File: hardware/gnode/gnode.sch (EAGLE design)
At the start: 20 parts, among them IC1 HTU21D, U1 ATMEGA328P_TQFP

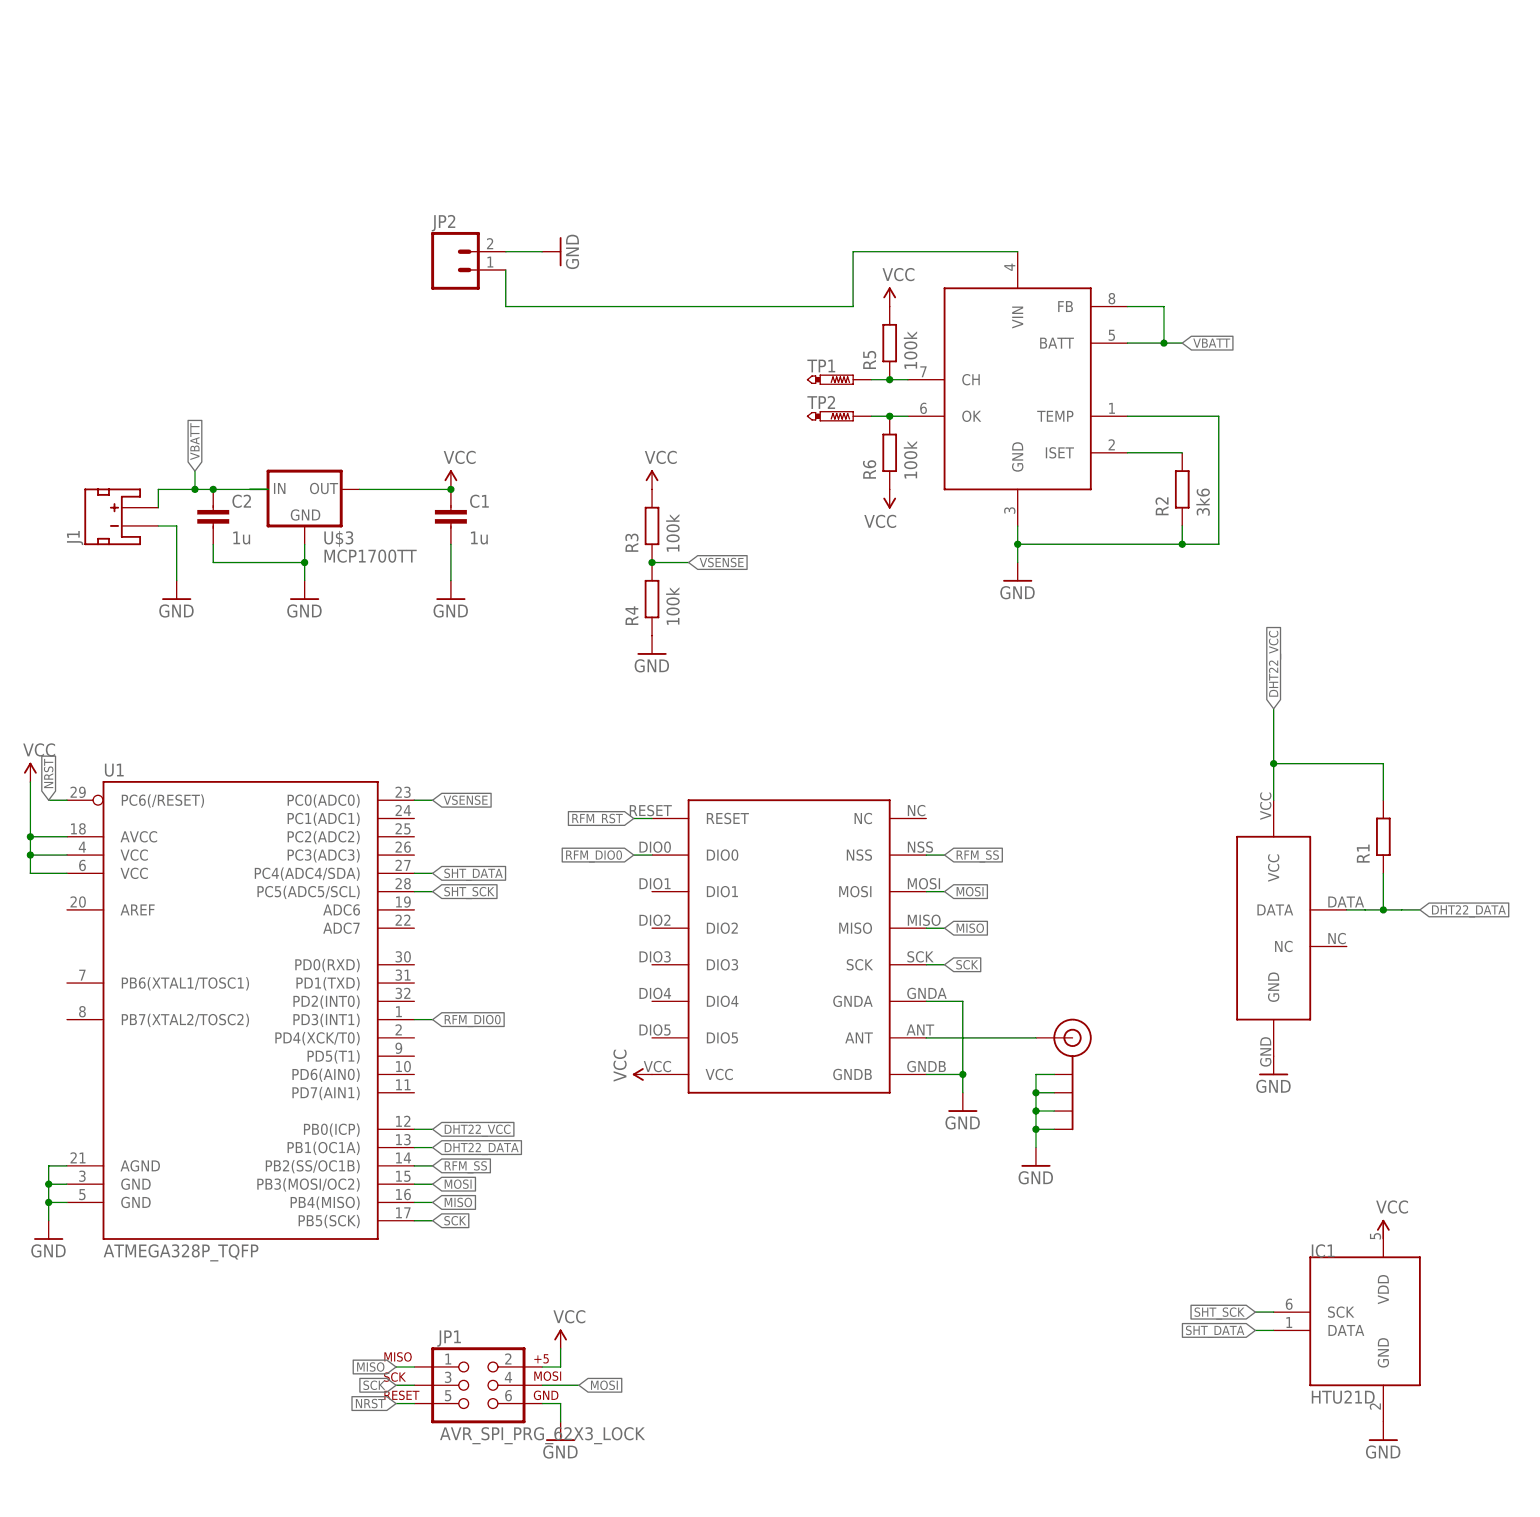
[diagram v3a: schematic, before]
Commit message: sense panel and battery voltages
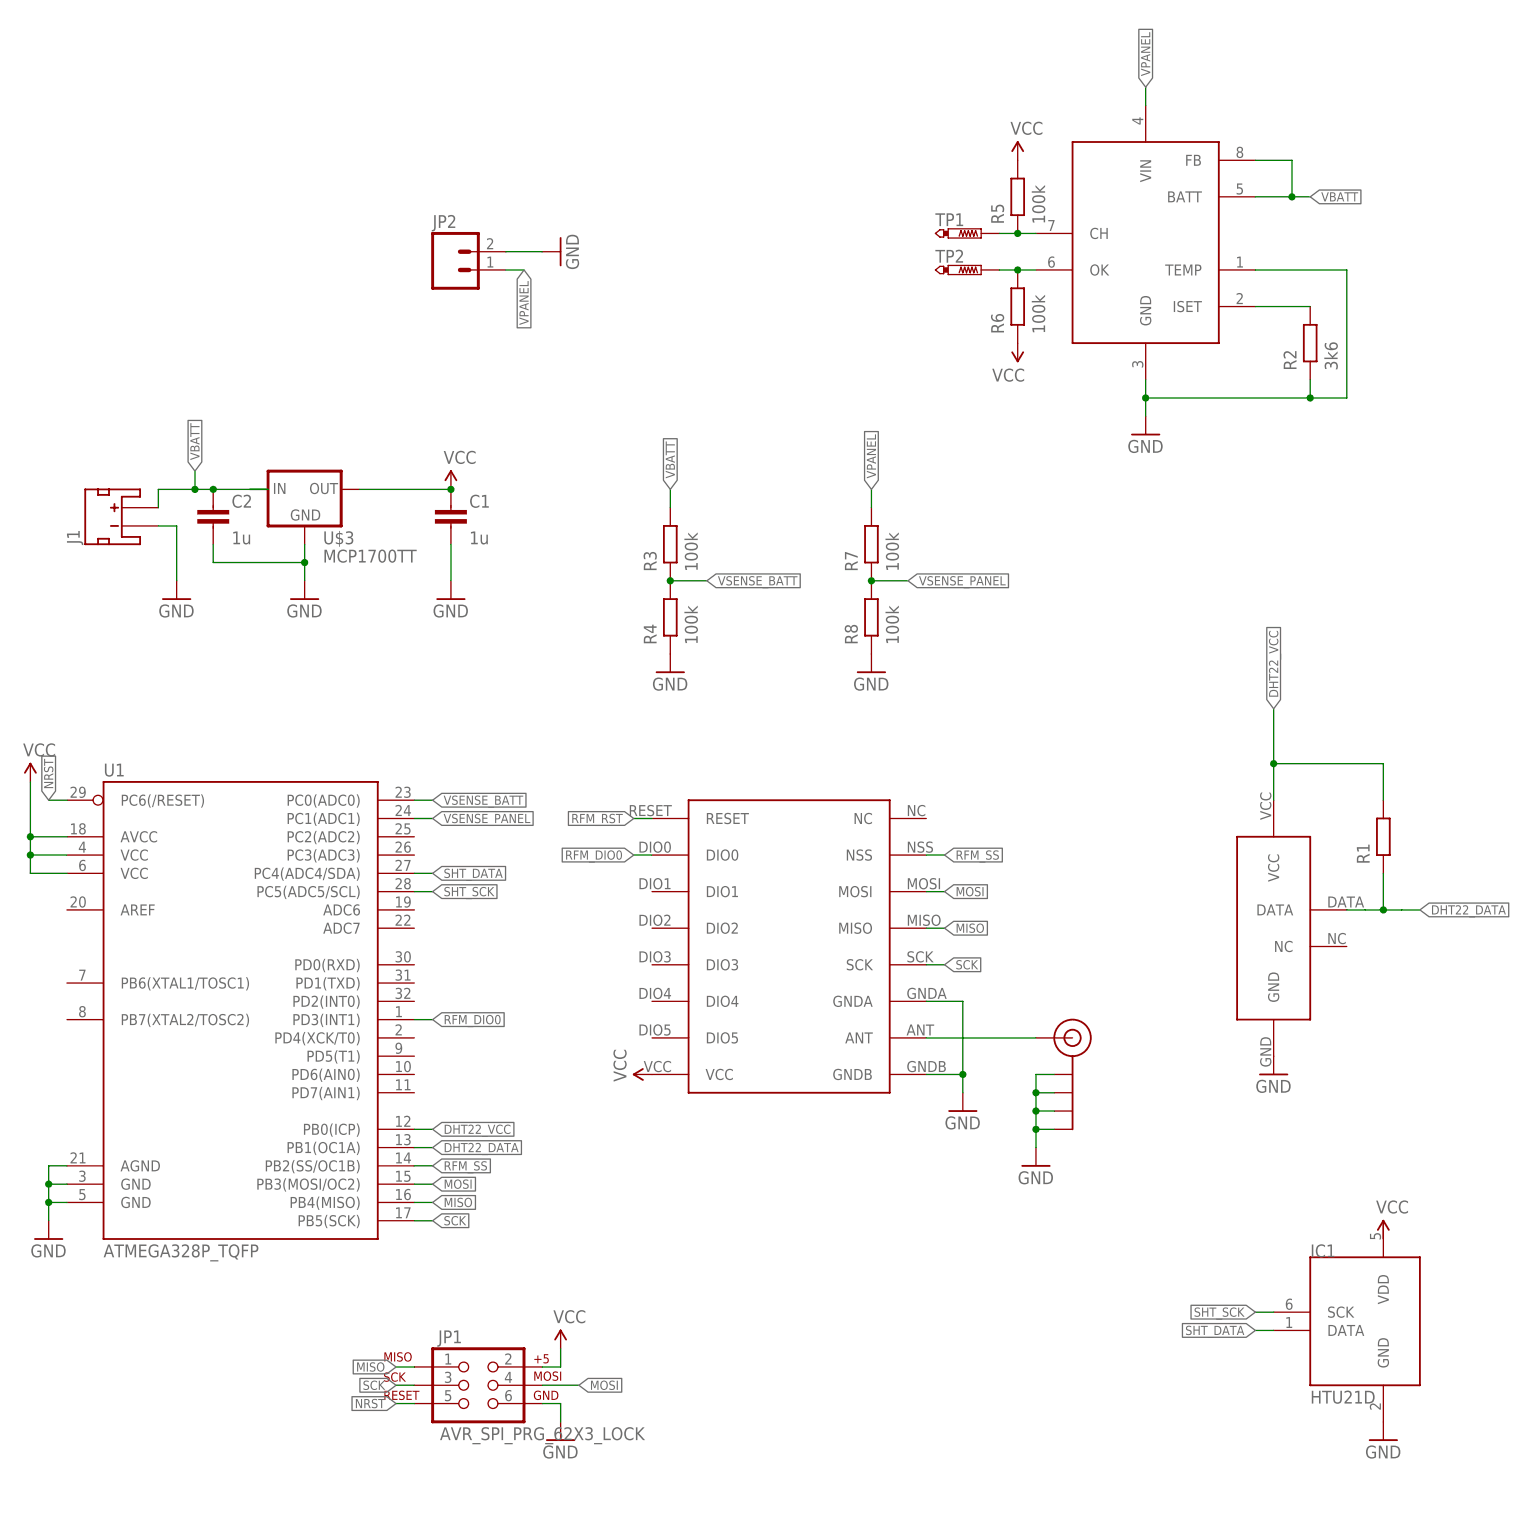
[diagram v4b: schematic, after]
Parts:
- added R7, R8: 100k, passives-7351:RESISTOR0603-N
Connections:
- net VSENSE renamed VSENSE_BATT
- removed net N$3: JP2.1, U$4.VIN
- new net VPANEL: JP2.1, R7.P$2, U$4.VIN
- new net VSENSE_PANEL: R7.P$1, R8.P$2, U1.PC1(ADC1)
- net GND: now also R8.P$1
- net VBATT: now also R3.P$2
- net VCC: no longer R3.P$2
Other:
- moved on the sheet: R2, R3, R4, R5, R6, TP1, TP2

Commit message: routed
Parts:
- removed U$2: DHT22_PTH, jonsowman:DHT22_PTH
- added C3: 100n, passives-7351:CAPACITOR0603-N
- added JP3: (no value), SparkFun-Connectors:M04PTH
- added U2: (no value), RHT03_DHT-22_AM2302:RHT03_DHT-22_AM2302
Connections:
- new net GPIO0: JP3.3, U1.PD6(AIN0)
- new net GPIO1: JP3.4, U1.PD7(AIN1)
- net DHT22_DATA: now also U2.DATA; no longer U$2.DATA
- net DHT22_VCC: now also U2.VDD; no longer U$2.VCC
- net GND: now also C3.2, JP3.2, U2.GND; no longer U$2.GND
- net VCC: now also C3.1, IC1.VDD, JP3.1
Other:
- moved on the sheet: IC1, R1
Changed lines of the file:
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@@
 <?xml version="1.0" encoding="utf-8"?>
 <!DOCTYPE eagle SYSTEM "eagle.dtd">
-<eagle version="6.6.0">
+<eagle version="6.5.0">
 <drawing>
 <settings>
@@
 <part name="U$1" library="hoperf" deviceset="RFM69HW" device=""/>
 <part name="U1" library="SparkFun-DigitalIC" deviceset="ATMEGA328P_TQFP" device="" value="ATMEGA328P_TQFP"/>
-<part name="U$2" library="jonsowman" deviceset="DHT22_PTH" device=""/>
 <part name="J$1" library="jonsowman" deviceset="SMA_EDGE" device=""/>
 <part name="GND1" library="SparkFun-Aesthetics" deviceset="GND" device=""/>
@@
 <part name="R7" library="passives-7351" deviceset="RESISTOR" device="0603-N" value="100k"/>
 <part name="R8" library="passives-7351" deviceset="RESISTOR" device="0603-N" value="100k"/>
+<part name="U2" library="RHT03_DHT-22_AM2302" deviceset="RHT03_DHT-22_AM2302" device=""/>
+<part name="C3" library="passives-7351" deviceset="CAPACITOR" device="0603-N" value="100n"/>
+<part name="JP3" library="SparkFun-Connectors" deviceset="M04" device="PTH"/>
 </parts>
 <sheets>
@@
 <instance part="U$1" gate="A" x="66.04" y="58.42"/>
 <instance part="U1" gate="U$1" x="-10.16" y="35.56"/>
-<instance part="U$2" gate="G$1" x="132.08" y="60.96"/>
 <instance part="J$1" gate="1" x="104.14" y="33.02"/>
-<instance part="GND1" gate="1" x="132.08" y="27.94"/>
+<instance part="GND1" gate="1" x="129.54" y="45.72"/>
 <instance part="GND2" gate="1" x="99.06" y="15.24"/>
 <instance part="GND3" gate="1" x="88.9" y="22.86"/>
-<instance part="R1" gate="G$1" x="147.32" y="60.96" rot="R90"/>
+<instance part="R1" gate="G$1" x="124.46" y="66.04" rot="R90"/>
 <instance part="SUPPLY1" gate="G$1" x="45.72" y="27.94" rot="R90"/>
 <instance part="SUPPLY2" gate="G$1" x="-40.64" y="68.58"/>
@@
 <instance part="SUPPLY3" gate="G$1" x="17.78" y="109.22"/>
 <instance part="GND7" gate="1" x="17.78" y="93.98"/>
-<instance part="IC1" gate="G$1" x="142.24" y="-7.62"/>
-<instance part="SUPPLY4" gate="G$1" x="147.32" y="5.08"/>
-<instance part="GND8" gate="1" x="147.32" y="-22.86"/>
+<instance part="IC1" gate="G$1" x="142.24" y="-10.16"/>
+<instance part="SUPPLY4" gate="G$1" x="147.32" y="15.24"/>
+<instance part="GND8" gate="1" x="147.32" y="-27.94"/>
 <instance part="JP1" gate="G$1" x="20.32" y="-15.24"/>
 <instance part="SUPPLY5" gate="G$1" x="33.02" y="-10.16"/>
@@
 <instance part="R7" gate="G$1" x="76.2" y="101.6" rot="R90"/>
 <instance part="R8" gate="G$1" x="76.2" y="91.44" rot="R90"/>
+<instance part="U2" gate="G$1" x="142.24" y="58.42"/>
+<instance part="C3" gate="G$1" x="-40.64" y="48.26"/>
+<instance part="JP3" gate="G$1" x="93.98" y="-15.24" rot="R180"/>
 </instances>
 <busses>
@@
 <nets>
 <net name="GND" class="0">
-<segment>
-<pinref part="U$2" gate="G$1" pin="GND"/>
-<pinref part="GND1" gate="1" pin="GND"/>
-</segment>
 <segment>
 <pinref part="J$1" gate="1" pin="GND@3"/>
@@
 <wire x1="-38.1" y1="15.24" x2="-38.1" y2="12.7" width="0.1524" layer="91"/>
 <junction x="-38.1" y="12.7"/>
+<pinref part="C3" gate="G$1" pin="2"/>
+<wire x1="-40.64" y1="43.18" x2="-38.1" y2="43.18" width="0.1524" layer="91"/>
+<wire x1="-38.1" y1="43.18" x2="-38.1" y2="15.24" width="0.1524" layer="91"/>
+<junction x="-38.1" y="15.24"/>
 </segment>
 <segment>
@@
 <pinref part="IC1" gate="G$1" pin="GND"/>
 <pinref part="GND8" gate="1" pin="GND"/>
+<wire x1="147.32" y1="-22.86" x2="147.32" y2="-25.4" width="0.1524" layer="91"/>
 </segment>
 <segment>
@@
 <pinref part="R8" gate="G$1" pin="P$1"/>
 </segment>
+<segment>
+<pinref part="U2" gate="G$1" pin="GND"/>
+<wire x1="132.08" y1="50.8" x2="129.54" y2="50.8" width="0.1524" layer="91"/>
+<pinref part="GND1" gate="1" pin="GND"/>
+<wire x1="129.54" y1="50.8" x2="129.54" y2="48.26" width="0.1524" layer="91"/>
+</segment>
+<segment>
+<pinref part="JP3" gate="G$1" pin="2"/>
+<wire x1="88.9" y1="-15.24" x2="86.36" y2="-15.24" width="0.1524" layer="91"/>
+<label x="86.36" y="-15.24" size="1.27" layer="95" rot="R180" xref="yes"/>
+</segment>
 </net>
 <net name="N$1" class="0">
@@
 <net name="DHT22_DATA" class="0">
 <segment>
-<pinref part="U$2" gate="G$1" pin="DATA"/>
-<wire x1="142.24" y1="50.8" x2="144.78" y2="50.8" width="0.1524" layer="91"/>
-<wire x1="144.78" y1="50.8" x2="147.32" y2="50.8" width="0.1524" layer="91"/>
-<wire x1="147.32" y1="50.8" x2="149.86" y2="50.8" width="0.1524" layer="91"/>
-<wire x1="149.86" y1="50.8" x2="152.4" y2="50.8" width="0.1524" layer="91"/>
+<wire x1="132.08" y1="60.96" x2="124.46" y2="60.96" width="0.1524" layer="91"/>
+<wire x1="124.46" y1="60.96" x2="121.92" y2="60.96" width="0.1524" layer="91"/>
 <pinref part="R1" gate="G$1" pin="P$1"/>
-<wire x1="147.32" y1="55.88" x2="147.32" y2="50.8" width="0.1524" layer="91"/>
-<junction x="147.32" y="50.8"/>
-<label x="152.4" y="50.8" size="1.27" layer="95" font="vector" xref="yes"/>
+<junction x="124.46" y="60.96"/>
+<label x="121.92" y="60.96" size="1.27" layer="95" font="vector" rot="R180" xref="yes"/>
+<pinref part="U2" gate="G$1" pin="DATA"/>
 </segment>
 <segment>
@@
 <net name="DHT22_VCC" class="0">
 <segment>
-<pinref part="U$2" gate="G$1" pin="VCC"/>
 <wire x1="132.08" y1="78.74" x2="132.08" y2="71.12" width="0.1524" layer="91"/>
 <pinref part="R1" gate="G$1" pin="P$2"/>
 <wire x1="132.08" y1="71.12" x2="132.08" y2="66.04" width="0.1524" layer="91"/>
-<wire x1="147.32" y1="66.04" x2="147.32" y2="71.12" width="0.1524" layer="91"/>
-<wire x1="147.32" y1="71.12" x2="132.08" y2="71.12" width="0.1524" layer="91"/>
+<wire x1="124.46" y1="71.12" x2="132.08" y2="71.12" width="0.1524" layer="91"/>
 <junction x="132.08" y="71.12"/>
 <label x="132.08" y="78.74" size="1.27" layer="95" font="vector" rot="R90" xref="yes"/>
+<pinref part="U2" gate="G$1" pin="VDD"/>
 </segment>
 <segment>
@@
 <wire x1="-40.64" y1="55.88" x2="-40.64" y2="58.42" width="0.1524" layer="91"/>
 <junction x="-40.64" y="58.42"/>
+<pinref part="C3" gate="G$1" pin="1"/>
+<wire x1="-40.64" y1="55.88" x2="-40.64" y2="50.8" width="0.1524" layer="91"/>
+<junction x="-40.64" y="55.88"/>
 </segment>
 <segment>
@@
 <pinref part="R6" gate="G$1" pin="P$1"/>
 <pinref part="SUPPLY8" gate="G$1" pin="VCC"/>
+</segment>
+<segment>
+<pinref part="IC1" gate="G$1" pin="VDD"/>
+<pinref part="SUPPLY4" gate="G$1" pin="VCC"/>
+<wire x1="147.32" y1="5.08" x2="147.32" y2="15.24" width="0.1524" layer="91"/>
+</segment>
+<segment>
+<pinref part="JP3" gate="G$1" pin="1"/>
+<wire x1="88.9" y1="-12.7" x2="86.36" y2="-12.7" width="0.1524" layer="91"/>
+<label x="86.36" y="-12.7" size="1.27" layer="95" rot="R180" xref="yes"/>
 </segment>
 </net>
@@
 <segment>
 <pinref part="IC1" gate="G$1" pin="SCK"/>
-<wire x1="132.08" y1="-5.08" x2="129.54" y2="-5.08" width="0.1524" layer="91"/>
-<label x="129.54" y="-5.08" size="1.27" layer="95" rot="R180" xref="yes"/>
+<wire x1="132.08" y1="-7.62" x2="129.54" y2="-7.62" width="0.1524" layer="91"/>
+<label x="129.54" y="-7.62" size="1.27" layer="95" rot="R180" xref="yes"/>
 </segment>
 <segment>
@@
 <segment>
 <pinref part="IC1" gate="G$1" pin="DATA"/>
-<wire x1="132.08" y1="-7.62" x2="129.54" y2="-7.62" width="0.1524" layer="91"/>
-<label x="129.54" y="-7.62" size="1.27" layer="95" rot="R180" xref="yes"/>
+<wire x1="132.08" y1="-10.16" x2="129.54" y2="-10.16" width="0.1524" layer="91"/>
+<label x="129.54" y="-10.16" size="1.27" layer="95" rot="R180" xref="yes"/>
 </segment>
 <segment>
@@
 </segment>
 </net>
+<net name="GPIO1" class="0">
+<segment>
+<pinref part="U1" gate="U$1" pin="PD7(AIN1)"/>
+<wire x1="12.7" y1="25.4" x2="15.24" y2="25.4" width="0.1524" layer="91"/>
+<label x="15.24" y="25.4" size="1.27" layer="95" xref="yes"/>
+</segment>
+<segment>
+<pinref part="JP3" gate="G$1" pin="4"/>
+<wire x1="88.9" y1="-20.32" x2="86.36" y2="-20.32" width="0.1524" layer="91"/>
+<label x="86.36" y="-20.32" size="1.27" layer="95" rot="R180" xref="yes"/>
+</segment>
+</net>
+<net name="GPIO0" class="0">
+<segment>
+<pinref part="U1" gate="U$1" pin="PD6(AIN0)"/>
+<wire x1="12.7" y1="27.94" x2="15.24" y2="27.94" width="0.1524" layer="91"/>
+<label x="15.24" y="27.94" size="1.27" layer="95" xref="yes"/>
+</segment>
+<segment>
+<pinref part="JP3" gate="G$1" pin="3"/>
+<wire x1="88.9" y1="-17.78" x2="86.36" y2="-17.78" width="0.1524" layer="91"/>
+<label x="86.36" y="-17.78" size="1.27" layer="95" rot="R180" xref="yes"/>
+</segment>
+</net>

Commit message: tidying
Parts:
- added C4: 100n, passives-7351:CAPACITOR0603-N
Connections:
- net GND: now also C4.2
- net VCC: now also C4.1
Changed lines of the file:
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@@
 <part name="C3" library="passives-7351" deviceset="CAPACITOR" device="0603-N" value="100n"/>
 <part name="JP3" library="SparkFun-Connectors" deviceset="M04" device="PTH"/>
+<part name="C4" library="passives-7351" deviceset="CAPACITOR" device="0603-N" value="100n"/>
 </parts>
 <sheets>
@@
 <instance part="C3" gate="G$1" x="-40.64" y="48.26"/>
 <instance part="JP3" gate="G$1" x="93.98" y="-15.24" rot="R180"/>
+<instance part="C4" gate="G$1" x="157.48" y="-7.62"/>
 </instances>
 <busses>
@@
 <pinref part="GND8" gate="1" pin="GND"/>
 <wire x1="147.32" y1="-22.86" x2="147.32" y2="-25.4" width="0.1524" layer="91"/>
+<pinref part="C4" gate="G$1" pin="2"/>
+<wire x1="157.48" y1="-12.7" x2="157.48" y2="-22.86" width="0.1524" layer="91"/>
+<wire x1="157.48" y1="-22.86" x2="147.32" y2="-22.86" width="0.1524" layer="91"/>
+<junction x="147.32" y="-22.86"/>
 </segment>
 <segment>
@@
 <pinref part="IC1" gate="G$1" pin="VDD"/>
 <pinref part="SUPPLY4" gate="G$1" pin="VCC"/>
-<wire x1="147.32" y1="5.08" x2="147.32" y2="15.24" width="0.1524" layer="91"/>
-</segment>
-<segment>
+<wire x1="147.32" y1="5.08" x2="147.32" y2="10.16" width="0.1524" layer="91"/>
+<wire x1="147.32" y1="10.16" x2="147.32" y2="15.24" width="0.1524" layer="91"/>
+<wire x1="147.32" y1="10.16" x2="157.48" y2="10.16" width="0.1524" layer="91"/>
+<wire x1="157.48" y1="10.16" x2="157.48" y2="-5.08" width="0.1524" layer="91"/>
+<junction x="147.32" y="10.16"/>
+<pinref part="C4" gate="G$1" pin="1"/>
+</segment>
+<segment>
